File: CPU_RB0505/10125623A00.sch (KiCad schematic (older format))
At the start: 23 parts

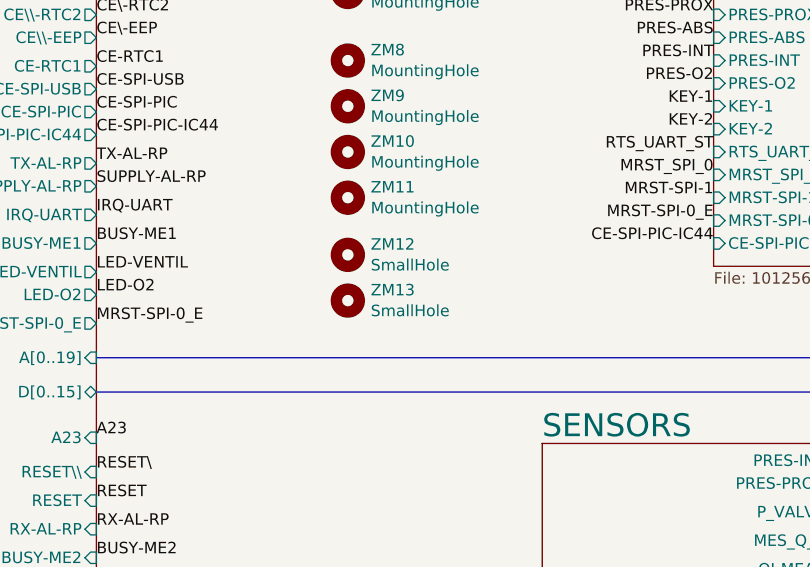
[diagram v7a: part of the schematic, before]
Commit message: rename fp and add 3d models
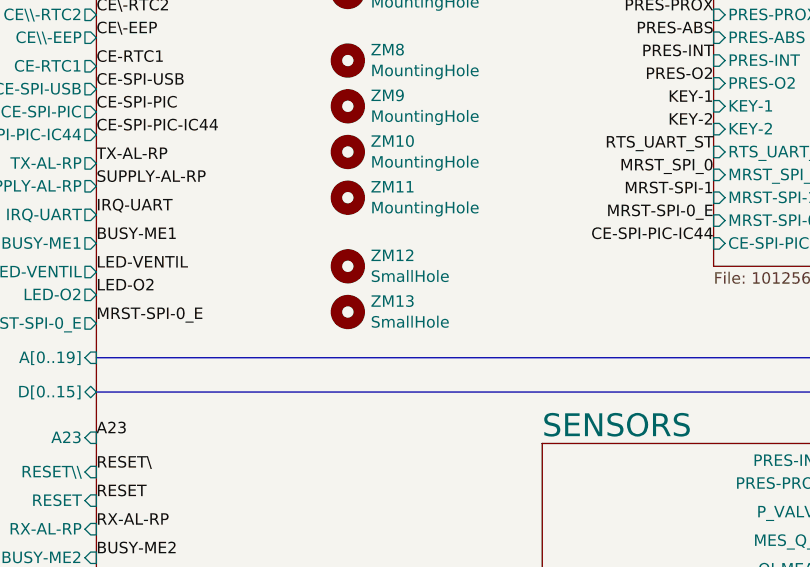
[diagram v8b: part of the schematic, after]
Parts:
- ZM10, ZM11, ZM8, ZM9: footprint AllModules:FIX35_1_display -> AllModules:FIX35_1_controller
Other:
- moved on the sheet: ZM12, ZM13
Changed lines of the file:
@@
 F 0 "ZM8" H 3150 4296 50  0000 L CNN
 F 1 "MountingHole" H 3150 4205 50  0000 L CNN
-F 2 "AllModules:FIX35_1_display" H 3050 4250 50  0001 C CNN
+F 2 "AllModules:FIX35_1_controller" H 3050 4250 50  0001 C CNN
 F 3 "~" H 3050 4250 50  0001 C CNN
 	1    3050 4250
@@
 F 0 "ZM9" H 3150 4496 50  0000 L CNN
 F 1 "MountingHole" H 3150 4405 50  0000 L CNN
-F 2 "AllModules:FIX35_1_display" H 3050 4450 50  0001 C CNN
+F 2 "AllModules:FIX35_1_controller" H 3050 4450 50  0001 C CNN
 F 3 "~" H 3050 4450 50  0001 C CNN
 	1    3050 4450
@@
 F 0 "ZM10" H 3150 4696 50  0000 L CNN
 F 1 "MountingHole" H 3150 4605 50  0000 L CNN
-F 2 "AllModules:FIX35_1_display" H 3050 4650 50  0001 C CNN
+F 2 "AllModules:FIX35_1_controller" H 3050 4650 50  0001 C CNN
 F 3 "~" H 3050 4650 50  0001 C CNN
 	1    3050 4650
@@
 F 0 "ZM11" H 3150 4896 50  0000 L CNN
 F 1 "MountingHole" H 3150 4805 50  0000 L CNN
-F 2 "AllModules:FIX35_1_display" H 3050 4850 50  0001 C CNN
+F 2 "AllModules:FIX35_1_controller" H 3050 4850 50  0001 C CNN
 F 3 "~" H 3050 4850 50  0001 C CNN
 	1    3050 4850
@@
 L Mechanical:MountingHole ZM12
 U 1 1 5EA85DF5
-P 3050 5100
-F 0 "ZM12" H 3150 5146 50  0000 L CNN
-F 1 "SmallHole" H 3150 5055 50  0000 L CNN
-F 2 "AllModules:FIX30_1" H 3050 5100 50  0001 C CNN
-F 3 "~" H 3050 5100 50  0001 C CNN
-	1    3050 5100
+P 3050 5150
+F 0 "ZM12" H 3150 5196 50  0000 L CNN
+F 1 "SmallHole" H 3150 5105 50  0000 L CNN
+F 2 "AllModules:FIX30_1" H 3050 5150 50  0001 C CNN
+F 3 "~" H 3050 5150 50  0001 C CNN
+	1    3050 5150
 	1    0    0    -1
 $EndComp
@@
 L Mechanical:MountingHole ZM13
 U 1 1 5EA87776
-P 3050 5300
-F 0 "ZM13" H 3150 5346 50  0000 L CNN
-F 1 "SmallHole" H 3150 5255 50  0000 L CNN
-F 2 "AllModules:FIX30_1" H 3050 5300 50  0001 C CNN
-F 3 "~" H 3050 5300 50  0001 C CNN
-	1    3050 5300
+P 3050 5350
+F 0 "ZM13" H 3150 5396 50  0000 L CNN
+F 1 "SmallHole" H 3150 5305 50  0000 L CNN
+F 2 "AllModules:FIX30_1" H 3050 5350 50  0001 C CNN
+F 3 "~" H 3050 5350 50  0001 C CNN
+	1    3050 5350
 	1    0    0    -1
 $EndComp
